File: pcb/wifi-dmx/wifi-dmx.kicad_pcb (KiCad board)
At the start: 2 copper layers, 2 parts, among them J3 USB4110GFA, J5 NC3FAH1

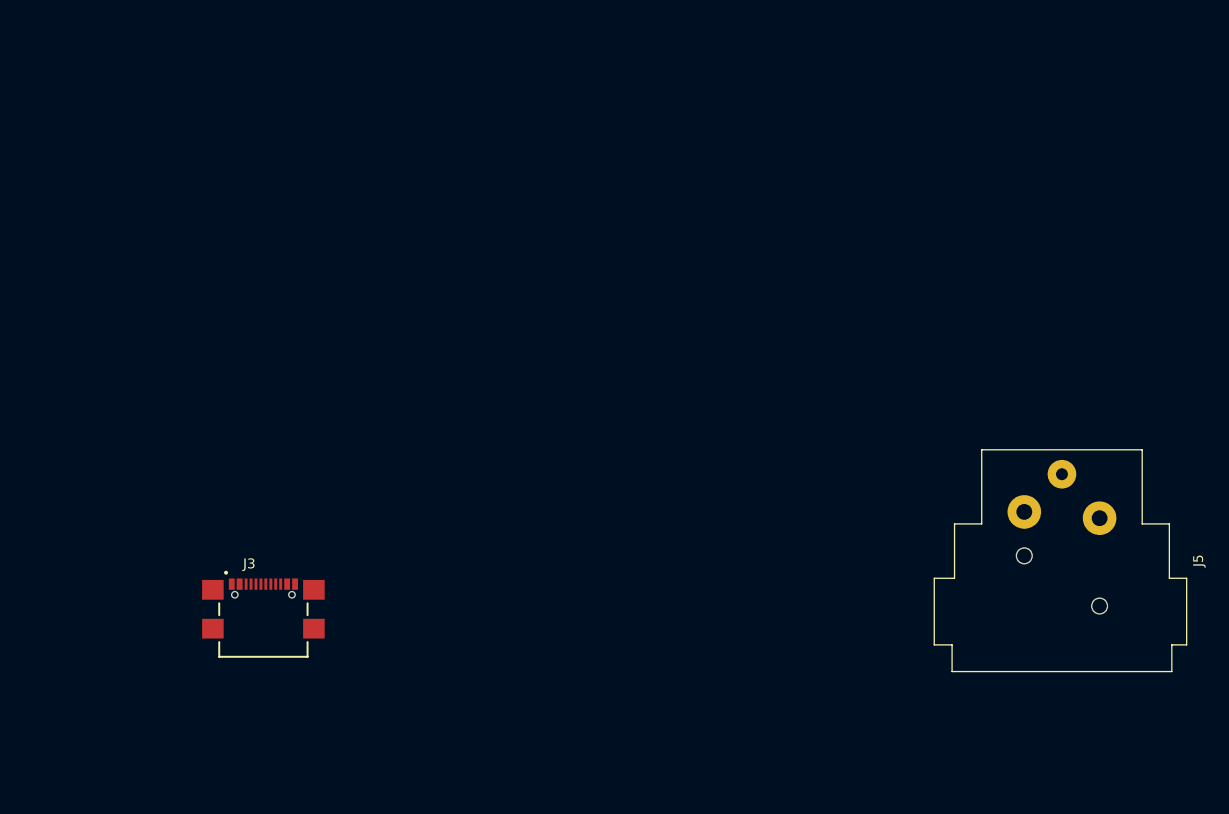
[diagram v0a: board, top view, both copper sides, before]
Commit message: finishing schematic and organizing pcb
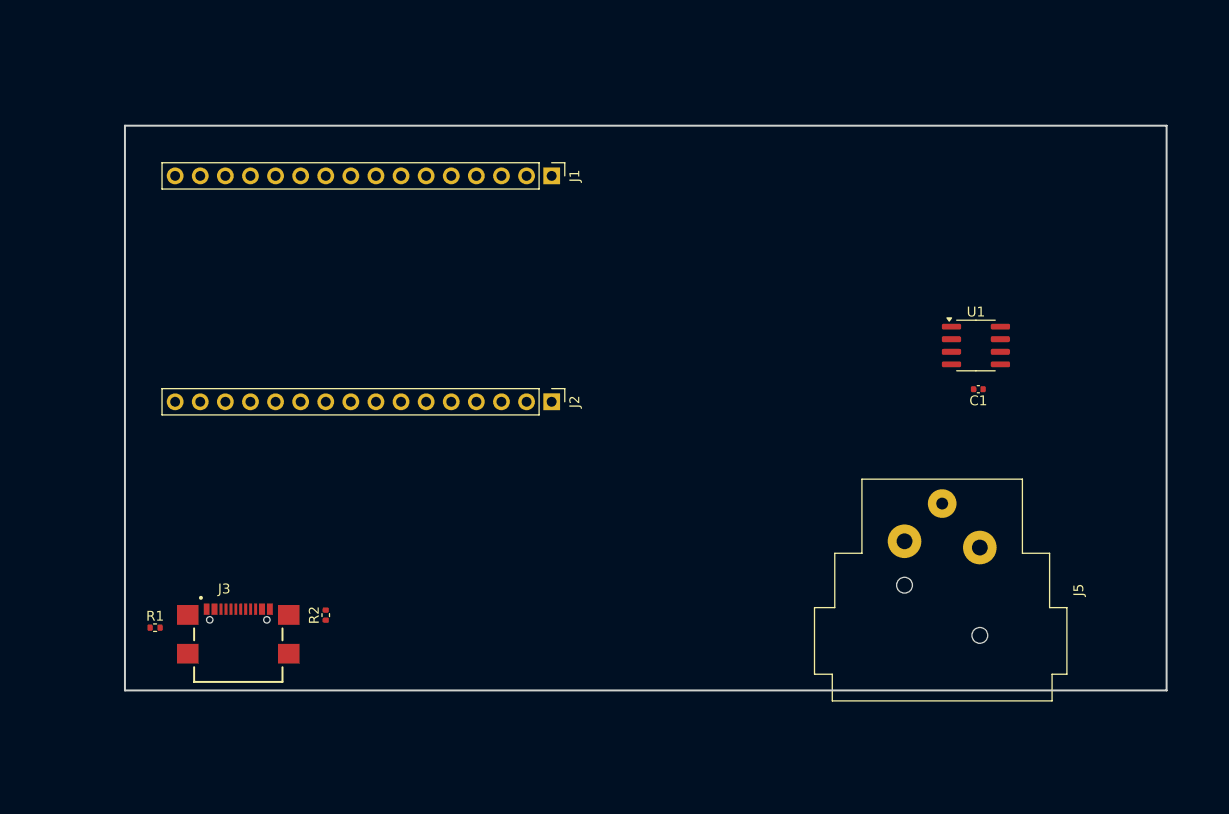
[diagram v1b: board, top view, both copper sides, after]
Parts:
- added C1: 0u1F, Capacitor_SMD:C_0402_1005Metric, F.Cu at (189.2, 99.1)
- added J1: Conn_01x16_Socket, Connector_PinHeader_2.54mm:PinHeader_1x16_P2.54mm_Vertical, F.Cu at (146.1, 77.5)
- added J2: Conn_01x16_Socket, Connector_PinHeader_2.54mm:PinHeader_1x16_P2.54mm_Vertical, F.Cu at (146.1, 100.3)
- added R1: 5k1, Resistor_SMD:R_0402_1005Metric, F.Cu at (105.9, 123.2)
- added R2: 5k1, Resistor_SMD:R_0402_1005Metric, F.Cu at (123.2, 121.9)
- added U1: MAX485E, Package_SO:SOIC-8_3.9x4.9mm_P1.27mm, F.Cu at (189.0, 94.6)
- moved J5 12.5 mm to (189.4, 115.1)
- moved J3 3.59 mm to (114.3, 122.4)
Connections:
- J5 pad 1: unconnected-(J5-Pad1) -> GND
- J5 pad 2: unconnected-(J5-Pad2) -> Net-(U1-B)
- J5 pad 3: unconnected-(J5-Pad3) -> Net-(U1-A)
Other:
- board outline added: 105.4 x 57.1 mm

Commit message: adding button and led to pcb
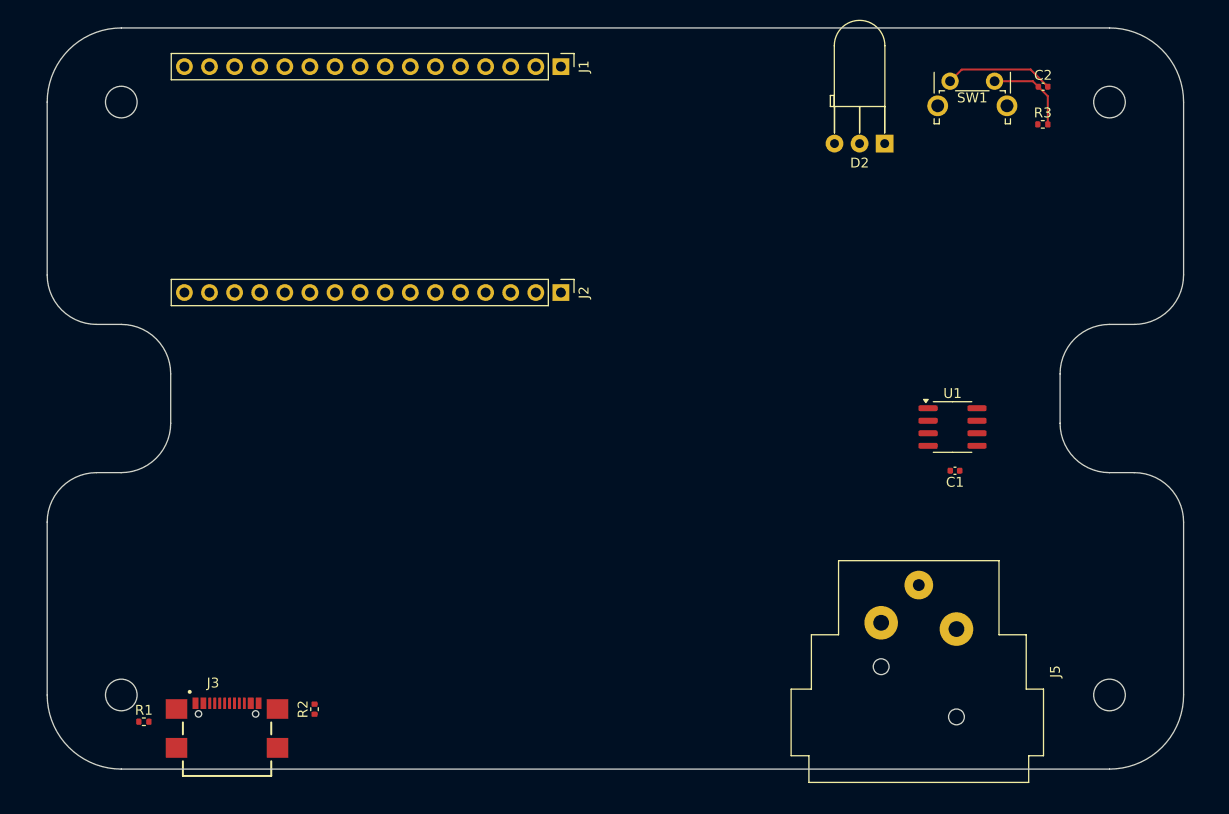
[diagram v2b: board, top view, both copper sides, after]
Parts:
- added C2: 0u1F, Capacitor_SMD:C_0402_1005Metric, F.Cu at (195.8, 68.4)
- added D2: LED_Dual_AKA, LED_THT:LED_D5.0mm-3_Horizontal_O3.81mm_Z3.0mm, F.Cu at (179.8, 74.2)
- added R3: 10k, Resistor_SMD:R_0402_1005Metric, F.Cu at (195.8, 72.3)
- added SW1: SW_Push, Button_Switch_THT:SW_Tactile_SPST_Angled_PTS645Vx58-2LFS, F.Cu at (186.4, 67.9)
- moved J1 11.1 mm to (147.0, 66.4)
- moved J2 11.1 mm to (147.0, 89.3)
- moved J3 9.59 mm to (113.2, 131.9)
- moved R1 9.59 mm to (104.8, 132.7)
- moved R2 9.59 mm to (122.1, 131.4)
- moved C1 8.58 mm to (186.9, 107.3)
- moved J5 8.58 mm to (187.0, 123.3)
- moved U1 8.58 mm to (186.6, 102.9)
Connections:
- J1 pad 2: unconnected-(J1-Pin_2-Pad2) -> VCC_3.3V
- J1 pad 3: unconnected-(J1-Pin_3-Pad3) -> BTN_BOOT
- J2 pad 3: unconnected-(J2-Pin_3-Pad3) -> LED
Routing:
- net GND: track 0.00 -> 11.1 mm
- net BTN_BOOT: track 0.00 -> 8.87 mm
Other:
- board size 105.4 x 57.1 mm -> 115 x 75 mm

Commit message: finishing schematic, finishing pcb, integrating pcb-stl with enclosure
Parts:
- added R4: 75R, Resistor_SMD:R_0402_1005Metric_Pad0.72x0.64mm_HandSolder, F.Cu at (106.7, 74.5)
- added R5: 75R, Resistor_SMD:R_0402_1005Metric_Pad0.72x0.64mm_HandSolder, F.Cu at (106.7, 79.5)
- C1, C2: footprint Capacitor_SMD:C_0402_1005Metric -> Capacitor_SMD:C_0402_1005Metric_Pad0.74x0.62mm_HandSolder
- R1, R2, R3: footprint Resistor_SMD:R_0402_1005Metric -> Resistor_SMD:R_0402_1005Metric_Pad0.72x0.64mm_HandSolder
- moved C2 93.4 mm to (104.1, 86.6)
- moved R3 92.5 mm to (104.1, 85.3), turned to 180 degrees
- moved SW1 90.7 mm to (98.2, 89.3), turned to 90 degrees
- moved D2 75.0 mm to (104.8, 74.5), turned to -90 degrees
- moved U1 11.7 mm to (179.5, 112.1)
- moved C1 11.0 mm to (179.6, 115.6), turned to 0 degrees
- moved R2 5.07 mm to (117.6, 133.9)
- moved J1 4.63 mm to (144.1, 70.0)
- moved J2 4.63 mm to (144.1, 92.9)
- moved J3 3.25 mm to (110.0, 132.4)
- moved R1 2.68 mm to (102.4, 133.9), turned to 90 degrees
- moved J5 1.14 mm to (186.8, 124.5)
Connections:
- J2 pad 3: LED -> LED_RED
- J2 pad 4: unconnected-(J2-Pin_4-Pad4) -> LED_GREEN
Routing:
- net VCC_5V: track 0.00 -> 113.8 mm
- net TXD1: track 0.00 -> 85.2 mm, vias 0 -> 2
- net VCC_3.3V: track 0.00 -> 56.2 mm
- net LED_RED: track 0.00 -> 47.1 mm
- net BTN_BOOT: track 8.87 -> 53.7 mm
- net D+: track 0.00 -> 41.7 mm
- net D-: track 0.00 -> 41.4 mm
- net LED_GREEN: track 0.00 -> 40.0 mm
- net Net-(U1-B): track 0.00 -> 19.3 mm
- net GND: track 11.1 -> 0.00 mm, vias 0 -> 16
- net Net-(U1-A): track 0.00 -> 9.11 mm
- net Net-(J3-CC1): track 0.00 -> 8.15 mm
- net Net-(J3-CC2): track 0.00 -> 7.66 mm
- net Net-(D2-A2): track 0.00 -> 2.19 mm
- net Net-(D2-A1): track 0.00 -> 2.15 mm
- added copper zone on B.Cu, net GND
- added copper zone on F.Cu, net GND
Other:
- board size 115 x 75 mm -> 114 x 70 mm

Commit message: adding board details on silkscreen
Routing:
- net VCC_5V: track 113.8 -> 119.8 mm, vias 0 -> 2
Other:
- board text added: "DESIGN BY SAMUEL HAFEN"
- board text added: "TRANCE wifi-dmx V0.1"
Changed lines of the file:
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@@
 		)
 		(property "Value" "NC3FAH1"
-			(at 4.3 18 90)
+			(at 16.55 3.81 0)
 			(layer "F.Fab")
 			(effects
@@
 		)
 		(fp_text user "${REFERENCE}"
-			(at 10.35 3.81 90)
+			(at 10.35 3.81 0)
 			(layer "F.Fab")
 			(effects
@@
 		)
 		(property "Value" "USB4110GFA"
-			(at 4.29 7.265 0)
+			(at 0 7.5625 0)
 			(layer "F.Fab")
 			(effects
@@
 		)
 		(property "Value" "Conn_01x16_Socket"
-			(at 0 40.43 90)
+			(at -4 19.05 0)
 			(layer "F.Fab")
 			(effects
@@
 		)
 		(property "Value" "SW_Push"
-			(at 2.275 5.6375 90)
+			(at 2.275 -7.2125 90)
 			(layer "F.Fab")
 			(effects
@@
 		)
 		(property "Value" "Conn_01x16_Socket"
-			(at 0 40.43 90)
+			(at -2.86 19.05 0)
 			(layer "F.Fab")
 			(effects
@@
 		(layer "Edge.Cuts")
 	)
+	(gr_text "TRANCE wifi-dmx V0.1"
+		(at 140.5 131 0)
+		(layer "F.SilkS")
+		(effects
+			(font
+				(size 1 1)
+				(thickness 0.1)
+			)
+			(justify left top)
+		)
+	)
+	(gr_text "DESIGN BY SAMUEL HAFEN"
+		(at 140.5 134 0)
+		(layer "F.SilkS")
+		(effects
+			(font
+				(size 1 1)
+				(thickness 0.1)
+			)
+			(justify left bottom)
+		)
+	)
 	(dimension
 		(type orthogonal)
@@
 		(layer "Cmts.User")
 		(pts
-			(xy 150 140) (xy 110 133)
+			(xy 150 140) (xy 110 138.7175)
 		)
 		(height 10)
@@
 	)
 	(segment
+		(start 107.6 130.4)
+		(end 108 130)
+		(width 0.2)
+		(layer "F.Cu")
+		(net 9)
+	)
+	(segment
 		(start 177 112.73)
 		(end 177.974999 112.73)
@@
 	)
 	(segment
+		(start 107.6 131.3625)
+		(end 107.6 130.4)
+		(width 0.2)
+		(layer "F.Cu")
+		(net 9)
+	)
+	(segment
 		(start 114.632 112.73)
 		(end 113.57 113.792)
@@
 	)
 	(segment
-		(start 113.57 113.792)
-		(end 113.57 128.492)
+		(start 177.974999 112.73)
+		(end 179.0105 113.765501)
 		(width 0.2)
 		(layer "F.Cu")
@@
 	)
 	(segment
-		(start 177.974999 112.73)
-		(end 179.0105 113.765501)
+		(start 177.601 110.859)
+		(end 181.281 110.859)
 		(width 0.2)
 		(layer "F.Cu")
@@
 	)
 	(segment
-		(start 177.601 110.859)
-		(end 181.281 110.859)
+		(start 113.57 92.86)
+		(end 113.57 113.792)
 		(width 0.2)
 		(layer "F.Cu")
@@
 	)
 	(segment
-		(start 112.4 129.662)
-		(end 112.4 131.3625)
+		(start 177 111.46)
+		(end 177.601 110.859)
 		(width 0.2)
 		(layer "F.Cu")
@@
 	)
 	(segment
-		(start 113.57 92.86)
-		(end 113.57 113.792)
+		(start 113.57 113.792)
+		(end 113.57 128.83)
 		(width 0.2)
 		(layer "F.Cu")
@@
 	)
 	(segment
-		(start 177 111.46)
-		(end 177.601 110.859)
+		(start 112.4 130)
+		(end 112.4 131.3625)
 		(width 0.2)
 		(layer "F.Cu")
@@
 	)
 	(segment
-		(start 113.57 128.492)
-		(end 112.4 129.662)
+		(start 113.57 128.83)
+		(end 112.4 130)
 		(width 0.2)
 		(layer "F.Cu")
 		(net 9)
 	)
+	(via
+		(at 108 130)
+		(size 0.6)
+		(drill 0.3)
+		(layers "F.Cu" "B.Cu")
+		(net 9)
+	)
+	(via
+		(at 112.4 130)
+		(size 0.6)
+		(drill 0.3)
+		(layers "F.Cu" "B.Cu")
+		(net 9)
+	)
+	(segment
+		(start 108 130)
+		(end 112.4 130)
+		(width 0.2)
+		(layer "B.Cu")
+		(net 9)
+	)
 	(segment
 		(start 98.7815 85.344)
@@
 	)
 	(zone
+		(net 0)
+		(net_name "")
+		(layer "F.Cu")
+		(hatch edge 0.5)
+		(connect_pads
+			(clearance 0)
+		)
+		(min_thickness 0.25)
+		(filled_areas_thickness no)
+		(keepout
+			(tracks not_allowed)
+			(vias not_allowed)
+			(pads not_allowed)
+			(copperpour not_allowed)
+			(footprints allowed)
+		)
+		(placement
+			(enabled no)
+			(sheetname "/")
+		)
+		(fill
+			(thermal_gap 0.5)
+			(thermal_bridge_width 0.5)
+		)
+		(polygon
+			(pts
+				(xy 139.5 130) (xy 161.5 130) (xy 161.5 135) (xy 139.5 135)
+			)
+		)
+	)
+	(zone
